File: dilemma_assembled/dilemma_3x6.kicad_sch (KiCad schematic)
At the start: 112 parts, among them J1 USB_C_Receptacle_USB2.0, J102 Serial, J103 Serial, J105 Conn_01x04_Female, J107 Conn_01x08_Female, J108 Conn_01x01_Female, J109 Conn_01x01_Female, J113 Cirque, J5 Conn_01x02, SW1 SW_Push, SW101 SW_Push, SW102 SW_Push, SW103 SW_Push, SW104 SW_Push, SW105 SW_Push, SW106 SW_Push, SW107 SW_Push, SW108 SW_Push, SW109 SW_Push, SW110 SW_SPST, SW111 SW_SPST, SW112 SW_Push, SW113 SW_Push, SW114 SW_Push, SW115 SW_Push, SW116 SW_Push, SW117 SW_Push, SW118 SW_Push, SW119 SW_Push, SW120 SW_Push, SW121 SW_Push, SW122 SW_Push, SW2 SW_Push, U1 RP2040, U2 GD25Q80CEIGR, U3 XC6210B332MR-G, Y1 Crystal_GND24

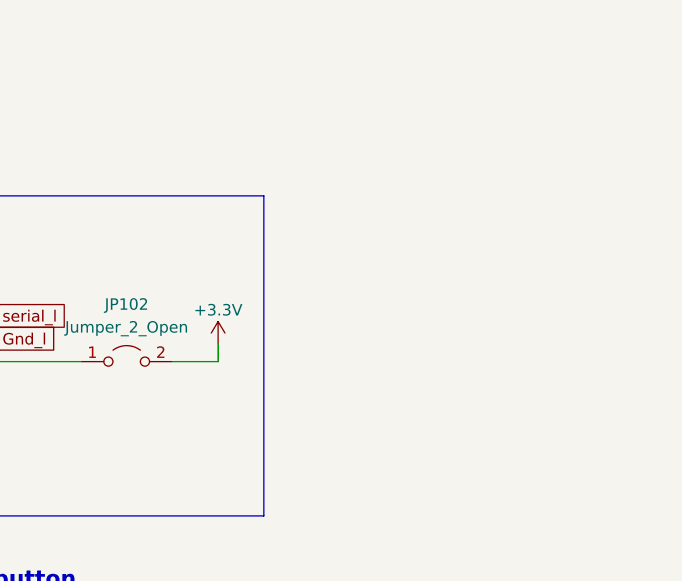
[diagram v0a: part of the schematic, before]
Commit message: add back puck
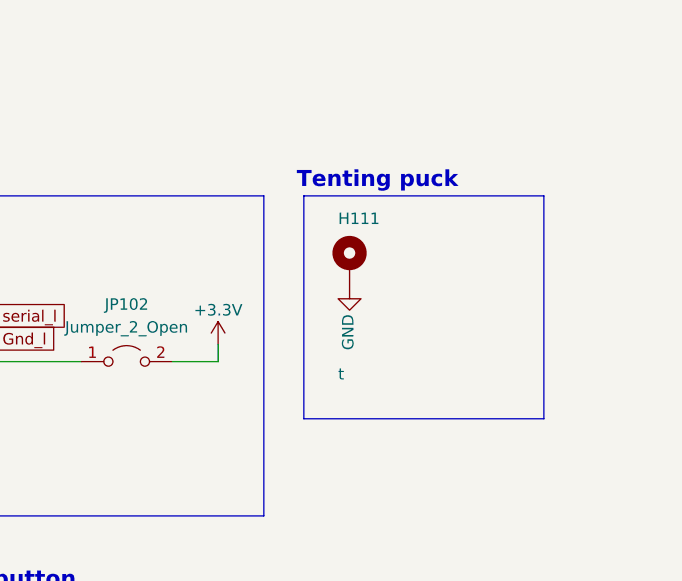
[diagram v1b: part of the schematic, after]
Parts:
- added H111: t, local-libraries:Tenting_Puck, symbol Mechanical:MountingHole_Pad
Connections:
- net GND: now also H111.1
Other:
- note added: "Tenting puck"
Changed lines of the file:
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@@
     (stroke (width 0) (type default) (color 0 0 0 0))
   )
+  (polyline (pts (xy 375.285 191.135) (xy 348.615 191.135))
+    (stroke (width 0) (type default) (color 0 0 0 0))
+  )
   (wire (pts (xy 267.97 127) (xy 256.54 127))
     (stroke (width 0) (type default) (color 0 0 0 0))
@@
     (stroke (width 0) (type default) (color 0 0 0 0))
   )
+  (polyline (pts (xy 348.615 166.37) (xy 348.615 191.135))
+    (stroke (width 0) (type default) (color 0 0 0 0))
+  )
   (wire (pts (xy 182.88 111.76) (xy 191.77 111.76))
     (stroke (width 0) (type default) (color 0 0 0 0))
@@
     (stroke (width 0) (type default) (color 0 0 0 0))
   )
+  (polyline (pts (xy 375.285 166.37) (xy 375.285 191.135))
+    (stroke (width 0) (type default) (color 0 0 0 0))
+  )
   (polyline (pts (xy 328.93 97.155) (xy 328.93 119.38))
     (stroke (width 0) (type default) (color 0 0 0 0))
@@
     (stroke (width 0) (type default) (color 0 0 0 0))
   )
+  (polyline (pts (xy 348.615 166.37) (xy 375.285 166.37))
+    (stroke (width 0) (type default) (color 0 0 0 0))
+  )
   (polyline (pts (xy 72.39 194.31) (xy 72.39 151.13))
     (stroke (width 0) (type default) (color 0 0 0 0))
@@
     (stroke (width 0) (type default) (color 0 0 0 0))
   )
+  (text "Tenting puck" (at 365.76 165.735 180)
+    (effects (font (size 1.778 1.778) (thickness 0.3556) bold) (justify right bottom))
+  )
   (text "Debug breakout" (at 285.115 97.155 0)
     (effects (font (size 1.778 1.778) (thickness 0.3556) bold) (justify left bottom))
@@
     (pin "2")
   )
+  (symbol (lib_id "Mechanical:MountingHole_Pad") (at 353.695 173.99 0) (unit 1)
+    (in_bom yes) (on_board yes)
+    (property "Reference" "H111" (id 0) (at 352.425 168.91 0)
+      (effects (font (size 1.27 1.27)) (justify left))
+    )
+    (property "Value" "t" (id 1) (at 352.425 186.182 0)
+      (effects (font (size 1.27 1.27)) (justify left))
+    )
+    (property "Footprint" "local-libraries:Tenting_Puck" (id 2) (at 353.695 173.99 0)
+      (effects (font (size 1.27 1.27)) hide)
+    )
+    (property "Datasheet" "~" (id 3) (at 353.695 173.99 0)
+      (effects (font (size 1.27 1.27)) hide)
+    )
+    (pin "1")
+  )
   (symbol (lib_id "Jumper:Jumper_2_Open") (at 313.69 61.595 0) (unit 1)
     (in_bom yes) (on_board yes) (fields_autoplaced)
@@
     (pin "1")
   )
+  (symbol (lib_id "power:GND") (at 353.695 176.53 0) (unit 1)
+    (in_bom yes) (on_board yes)
+    (property "Reference" "#PWR0124" (id 0) (at 353.695 182.88 0)
+      (effects (font (size 1.27 1.27)) hide)
+    )
+    (property "Value" "GND" (id 1) (at 353.539 183.5149 90)
+      (effects (font (size 1.27 1.27)) (justify left))
+    )
+    (property "Footprint" "" (id 2) (at 353.695 176.53 0)
+      (effects (font (size 1.27 1.27)) hide)
+    )
+    (property "Datasheet" "" (id 3) (at 353.695 176.53 0)
+      (effects (font (size 1.27 1.27)) hide)
+    )
+    (pin "1")
+  )
   (symbol (lib_id "power:GND") (at 55.245 186.055 0) (unit 1)
     (in_bom yes) (on_board yes)
@@
       (reference "#PWR0123") (unit 1) (value "GND") (footprint "")
     )
+    (path "/096216c5-6902-43a5-8004-8a4114c8baa4"
+      (reference "#PWR0124") (unit 1) (value "GND") (footprint "")
+    )
     (path "/4a21e78b-0ab0-4b88-8132-9b174e045719"
       (reference "C1") (unit 1) (value "1µ") (footprint "Capacitor_SMD:C_0603_1608Metric")
@@
       (reference "H110") (unit 1) (value "t") (footprint "local-libraries:JLC_SMT_Assembly_Hole")
     )
+    (path "/0432f300-18af-426a-9b34-ad1ec300821d"
+      (reference "H111") (unit 1) (value "t") (footprint "local-libraries:Tenting_Puck")
+    )
     (path "/6125bb34-31fe-49ed-b2ab-61dab24d450a"
